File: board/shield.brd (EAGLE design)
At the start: 66 x 57.8 mm, 45 parts, among them IC1 LM75, J1 22-05-7048-04, J2 22-05-7028-02, J4 POWER_JACKPTH, K1 G5L, T1 BC817, U1 LM2596S-5.0

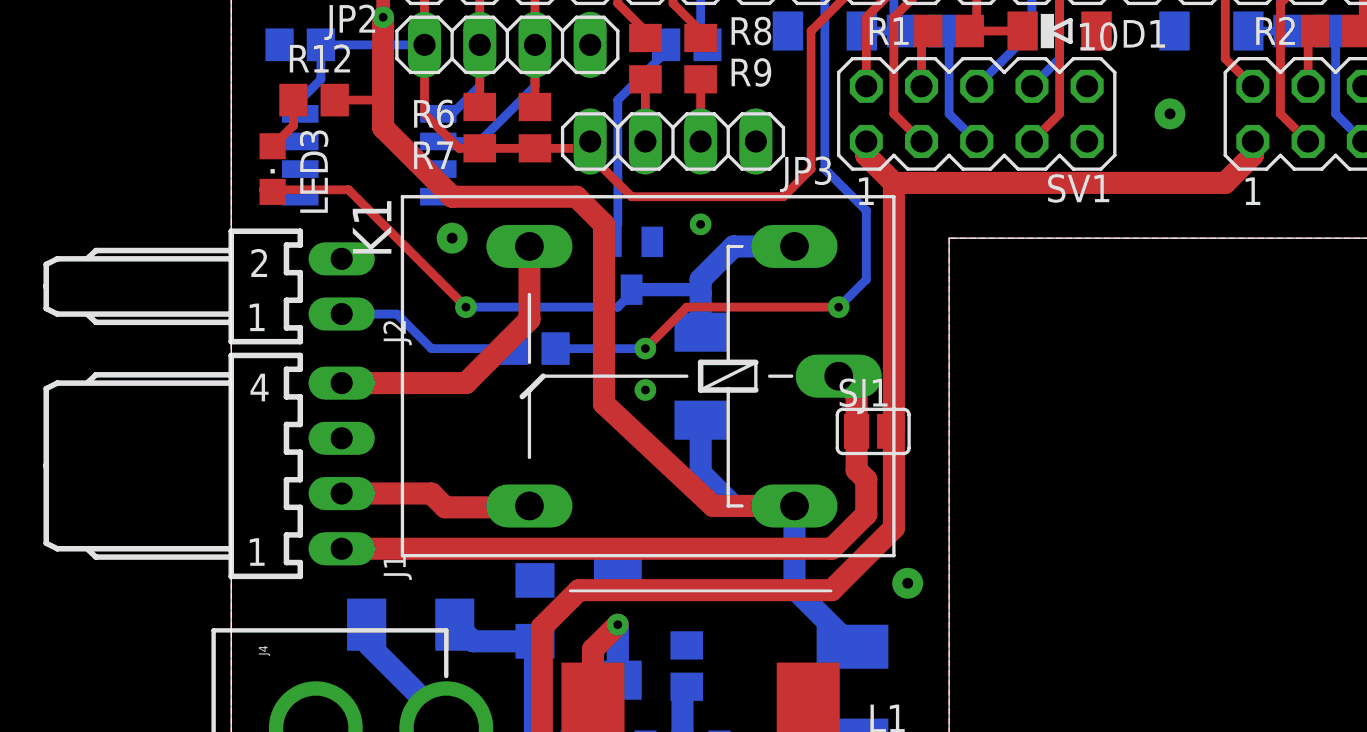
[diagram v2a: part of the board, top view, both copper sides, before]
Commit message: Fixed DRC Error, minor changes
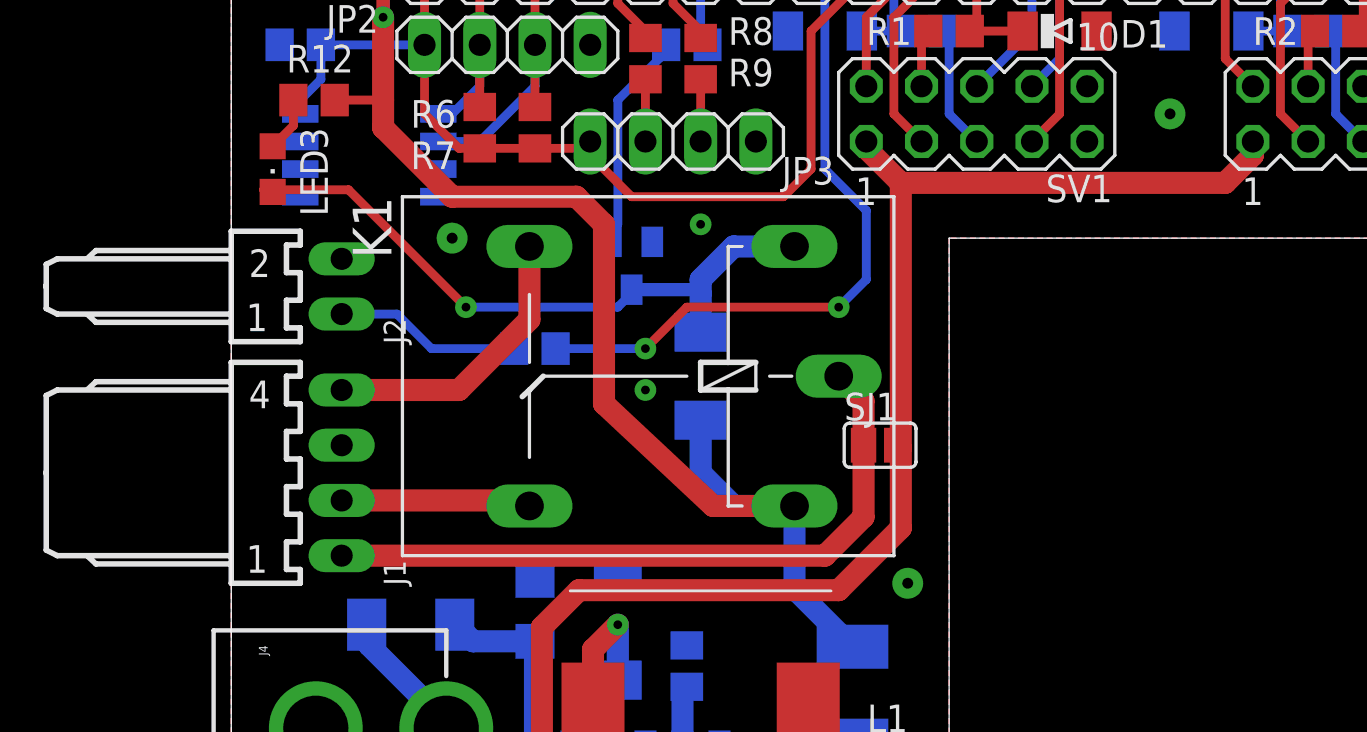
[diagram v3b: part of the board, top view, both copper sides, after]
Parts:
- moved SJ1 0.71 mm to (29.8, 30.5)
- moved J1 0.32 mm to (5.08, 29.2)
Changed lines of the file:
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@@
 <attribute name="PROD_ID" value="CONN-08197" x="-3.81" y="17.4625" size="1.778" layer="27" rot="R270" display="off"/>
 </element>
-<element name="J1" library="con-molex" package="7395-04" value="22-05-7048-04" x="5.08" y="29.5275" rot="R270">
-<attribute name="MF" value="" x="5.08" y="29.5275" size="1.778" layer="27" rot="R270" display="off"/>
-<attribute name="MPN" value="" x="5.08" y="29.5275" size="1.778" layer="27" rot="R270" display="off"/>
-<attribute name="OC_FARNELL" value="unknown" x="5.08" y="29.5275" size="1.778" layer="27" rot="R270" display="off"/>
-<attribute name="OC_NEWARK" value="unknown" x="5.08" y="29.5275" size="1.778" layer="27" rot="R270" display="off"/>
+<element name="J1" library="con-molex" package="7395-04" value="22-05-7048-04" x="5.08" y="29.21" rot="R270">
+<attribute name="MF" value="" x="5.08" y="29.21" size="1.778" layer="27" rot="R270" display="off"/>
+<attribute name="MPN" value="" x="5.08" y="29.21" size="1.778" layer="27" rot="R270" display="off"/>
+<attribute name="OC_FARNELL" value="unknown" x="5.08" y="29.21" size="1.778" layer="27" rot="R270" display="off"/>
+<attribute name="OC_NEWARK" value="unknown" x="5.08" y="29.21" size="1.778" layer="27" rot="R270" display="off"/>
 </element>
-<element name="SJ1" library="jumper" package="SJ" value="" x="29.5275" y="31.115"/>
+<element name="SJ1" library="jumper" package="SJ" value="" x="29.845" y="30.48"/>
 </elements>
 <signals>
@@
 <contactref element="SV1" pad="1"/>
 <contactref element="SV2" pad="1"/>
-<wire x1="29.21" y1="43.815" x2="30.48" y2="42.545" width="1.016" layer="1"/>
-<wire x1="29.21" y1="44.45" x2="29.21" y2="43.815" width="1.016" layer="1"/>
+<wire x1="29.21" y1="44.1325" x2="30.7975" y2="42.545" width="1.016" layer="1"/>
+<wire x1="29.21" y1="44.45" x2="29.21" y2="44.1325" width="1.016" layer="1"/>
 <wire x1="46.99" y1="44.45" x2="46.99" y2="43.815" width="1.016" layer="1"/>
 <wire x1="46.99" y1="43.815" x2="45.72" y2="42.545" width="1.016" layer="1"/>
-<wire x1="45.72" y1="42.545" x2="30.48" y2="42.545" width="1.016" layer="1"/>
-<wire x1="30.48" y1="42.545" x2="30.48" y2="31.4325" width="1.016" layer="1"/>
-<wire x1="30.48" y1="31.3055" x2="30.48" y2="26.67" width="1.016" layer="1"/>
-<wire x1="30.48" y1="26.67" x2="27.6225" y2="23.8125" width="1.016" layer="1"/>
-<wire x1="15.995" y1="23.8125" x2="27.6225" y2="23.8125" width="1.016" layer="1"/>
+<wire x1="45.72" y1="42.545" x2="30.7975" y2="42.545" width="1.016" layer="1"/>
+<wire x1="30.7975" y1="42.545" x2="30.7975" y2="30.353" width="1.016" layer="1"/>
+<wire x1="30.7975" y1="30.353" x2="30.7975" y2="26.67" width="1.016" layer="1"/>
+<wire x1="30.7975" y1="26.67" x2="27.94" y2="23.8125" width="1.016" layer="1"/>
+<wire x1="15.995" y1="23.8125" x2="27.94" y2="23.8125" width="1.016" layer="1"/>
 <wire x1="12.065" y1="9.4742" x2="12.065" y2="12.065" width="1.016" layer="1"/>
 <wire x1="11.125" y1="21.46" x2="10.36" y2="22.225" width="1.016" layer="16"/>
@@
 <wire x1="10.36" y1="22.225" x2="10.28" y2="22.225" width="0.4064" layer="16"/>
 <contactref element="SJ1" pad="2"/>
-<wire x1="30.2895" y1="31.115" x2="30.48" y2="31.3055" width="1.016" layer="1"/>
-<wire x1="30.48" y1="31.3055" x2="30.48" y2="31.4325" width="1.016" layer="1"/>
+<wire x1="30.607" y1="30.48" x2="30.7975" y2="30.353" width="1.016" layer="1"/>
 </signal>
 <signal name="N$4">
@@
 <signal name="NO">
 <contactref element="K1" pad="S"/>
-<wire x1="5.08" y1="33.3375" x2="10.795" y2="33.3375" width="1.016" layer="1"/>
-<wire x1="10.795" y1="33.3375" x2="13.716" y2="36.2585" width="1.016" layer="1"/>
+<wire x1="5.08" y1="33.02" x2="10.4775" y2="33.02" width="1.016" layer="1"/>
+<wire x1="10.4775" y1="33.02" x2="13.716" y2="36.2585" width="1.016" layer="1"/>
 <wire x1="13.716" y1="36.2585" x2="13.716" y2="39.624" width="1.016" layer="1"/>
 <contactref element="J1" pad="4"/>
@@
 <signal name="NC">
 <contactref element="K1" pad="O"/>
-<wire x1="5.08" y1="28.2575" x2="9.2075" y2="28.2575" width="1.016" layer="1"/>
-<wire x1="9.2075" y1="28.2575" x2="9.8425" y2="27.6225" width="1.016" layer="1"/>
-<wire x1="9.8425" y1="27.6225" x2="13.6525" y2="27.6225" width="1.016" layer="1"/>
-<wire x1="13.6525" y1="27.6225" x2="13.716" y2="27.686" width="1.016" layer="1"/>
+<wire x1="5.08" y1="27.94" x2="13.335" y2="27.94" width="1.016" layer="1"/>
+<wire x1="13.335" y1="27.94" x2="13.716" y2="27.686" width="1.016" layer="1"/>
 <contactref element="J1" pad="2"/>
 </signal>
@@
 <contactref element="J1" pad="1"/>
 <contactref element="SJ1" pad="1"/>
-<wire x1="5.08" y1="25.7175" x2="27.6225" y2="25.7175" width="1.016" layer="1"/>
-<wire x1="27.6225" y1="25.7175" x2="29.21" y2="27.305" width="1.016" layer="1"/>
-<wire x1="29.21" y1="27.305" x2="29.21" y2="28.8925" width="1.016" layer="1"/>
-<wire x1="29.21" y1="28.8925" x2="28.7655" y2="29.337" width="1.016" layer="1"/>
-<wire x1="28.7655" y1="29.337" x2="28.7655" y2="31.115" width="1.016" layer="1"/>
-<wire x1="27.94" y1="33.655" x2="28.7655" y2="32.8295" width="1.016" layer="1"/>
-<wire x1="28.7655" y1="32.8295" x2="28.7655" y2="31.115" width="1.016" layer="1"/>
+<wire x1="5.08" y1="25.4" x2="27.305" y2="25.4" width="1.016" layer="1"/>
+<wire x1="29.083" y1="30.2895" x2="29.083" y2="30.48" width="1.016" layer="1"/>
+<wire x1="27.305" y1="25.4" x2="29.083" y2="27.178" width="1.016" layer="1"/>
+<wire x1="29.083" y1="27.178" x2="29.083" y2="30.48" width="1.016" layer="1"/>
+<wire x1="29.083" y1="30.48" x2="29.083" y2="32.512" width="1.016" layer="1"/>
+<wire x1="29.083" y1="32.512" x2="27.94" y2="33.655" width="1.016" layer="1"/>
 </signal>
 </signals>

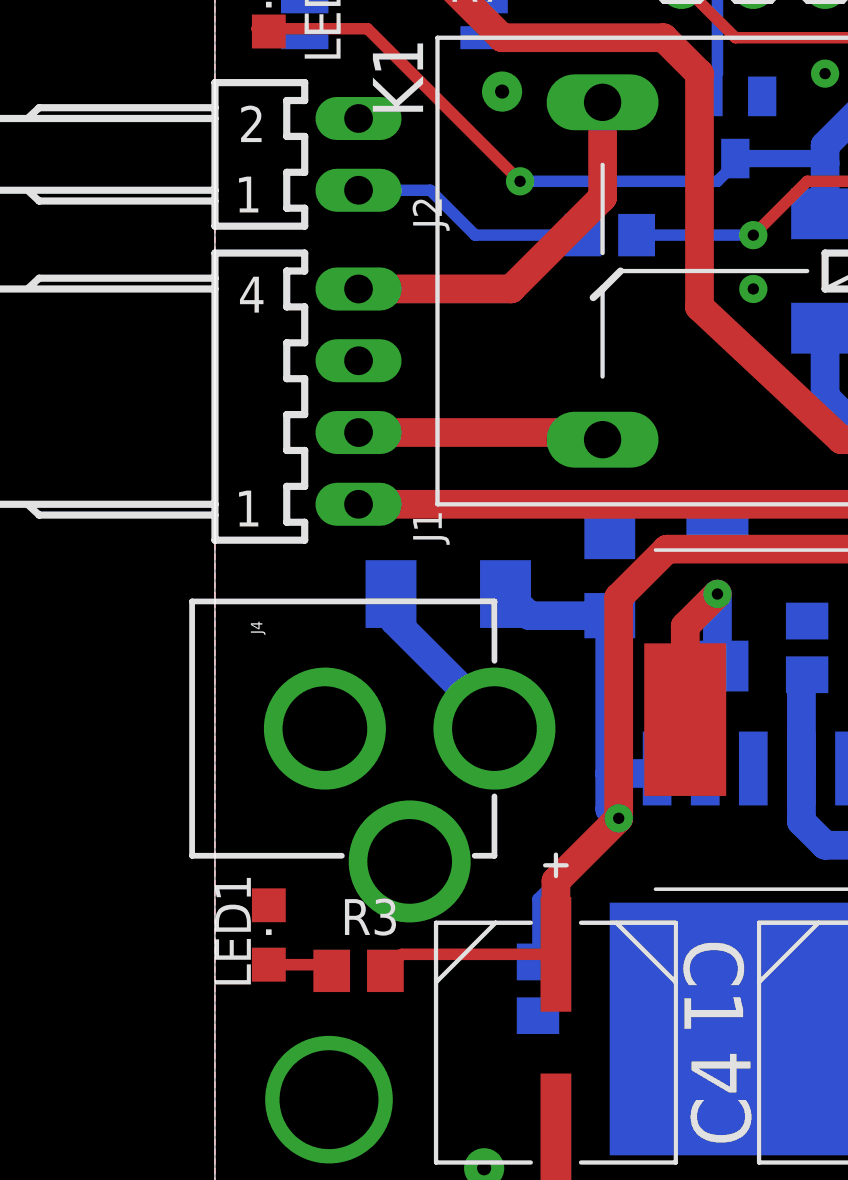
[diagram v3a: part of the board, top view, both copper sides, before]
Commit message: Labels position optimized
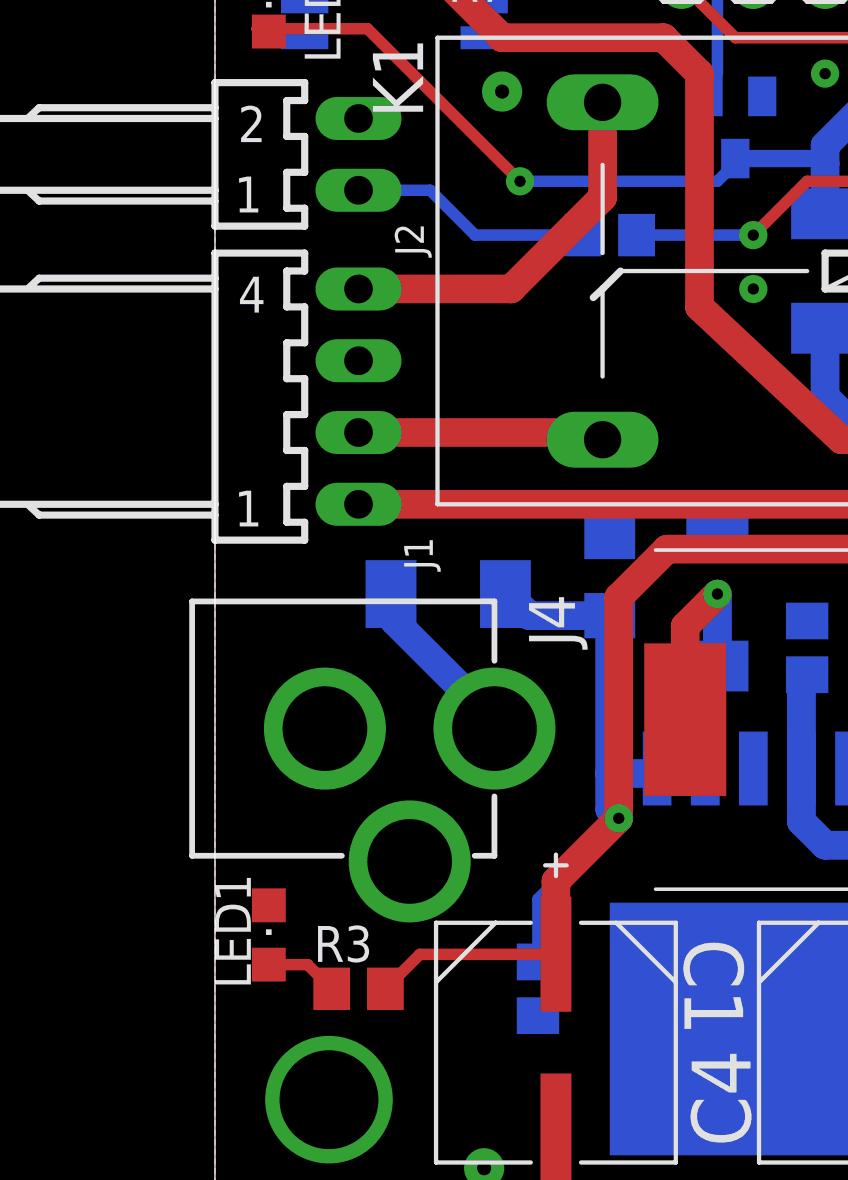
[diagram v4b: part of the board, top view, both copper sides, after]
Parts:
- moved R3 0.63 mm to (5.08, 8.26)
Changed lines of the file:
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@@
 <layers>
 <layer number="1" name="Top" color="4" fill="1" visible="yes" active="yes"/>
-<layer number="16" name="Bottom" color="1" fill="1" visible="yes" active="yes"/>
+<layer number="16" name="Bottom" color="1" fill="1" visible="no" active="yes"/>
 <layer number="17" name="Pads" color="2" fill="1" visible="yes" active="yes"/>
 <layer number="18" name="Vias" color="2" fill="1" visible="yes" active="yes"/>
@@
 <layer number="20" name="Dimension" color="15" fill="1" visible="yes" active="yes"/>
 <layer number="21" name="tPlace" color="7" fill="1" visible="yes" active="yes"/>
-<layer number="22" name="bPlace" color="7" fill="1" visible="yes" active="yes"/>
+<layer number="22" name="bPlace" color="7" fill="1" visible="no" active="yes"/>
 <layer number="23" name="tOrigins" color="15" fill="1" visible="yes" active="yes"/>
-<layer number="24" name="bOrigins" color="15" fill="1" visible="yes" active="yes"/>
-<layer number="25" name="tNames" color="7" fill="1" visible="no" active="yes"/>
+<layer number="24" name="bOrigins" color="15" fill="1" visible="no" active="yes"/>
+<layer number="25" name="tNames" color="7" fill="1" visible="yes" active="yes"/>
 <layer number="26" name="bNames" color="7" fill="1" visible="no" active="yes"/>
 <layer number="27" name="tValues" color="7" fill="1" visible="no" active="yes"/>
@@
 <layer number="50" name="dxf" color="7" fill="1" visible="no" active="no"/>
 <layer number="51" name="tDocu" color="7" fill="1" visible="yes" active="yes"/>
-<layer number="52" name="bDocu" color="7" fill="1" visible="yes" active="yes"/>
+<layer number="52" name="bDocu" color="7" fill="1" visible="no" active="yes"/>
 <layer number="53" name="tPadExt" color="7" fill="1" visible="no" active="no"/>
 <layer number="54" name="bPadExt" color="1" fill="1" visible="no" active="no"/>
@@
 <layer number="99" name="SpiceOrder" color="5" fill="1" visible="no" active="no"/>
 <layer number="100" name="Muster" color="7" fill="1" visible="no" active="no"/>
-<layer number="101" name="Patch_Top" color="12" fill="4" visible="yes" active="yes"/>
-<layer number="102" name="Vscore" color="7" fill="1" visible="yes" active="yes"/>
-<layer number="103" name="tMap" color="7" fill="1" visible="yes" active="yes"/>
-<layer number="104" name="Name" color="16" fill="1" visible="yes" active="yes"/>
+<layer number="101" name="Patch_Top" color="12" fill="4" visible="no" active="yes"/>
+<layer number="102" name="Vscore" color="7" fill="1" visible="no" active="yes"/>
+<layer number="103" name="tMap" color="7" fill="1" visible="no" active="yes"/>
+<layer number="104" name="Name" color="16" fill="1" visible="no" active="yes"/>
 <layer number="105" name="tPlate" color="7" fill="1" visible="yes" active="yes"/>
-<layer number="106" name="bPlate" color="7" fill="1" visible="yes" active="yes"/>
+<layer number="106" name="bPlate" color="7" fill="1" visible="no" active="yes"/>
 <layer number="107" name="Crop" color="7" fill="1" visible="yes" active="yes"/>
 <layer number="108" name="tplace-old" color="10" fill="1" visible="yes" active="yes"/>
@@
 <attribute name="VALUE" x="16.51" y="41.91" size="1.27" layer="28" rot="MR180"/>
 </element>
-<element name="R3" library="rcl" package="R0805" value="5K6" x="5.08" y="8.89" smashed="yes">
-<attribute name="NAME" x="4.445" y="10.16" size="1.27" layer="25"/>
-<attribute name="VALUE" x="4.445" y="6.35" size="1.27" layer="27"/>
+<element name="R3" library="rcl" package="R0805" value="5K6" x="5.08" y="8.255" smashed="yes">
+<attribute name="NAME" x="3.4925" y="9.2075" size="1.27" layer="25"/>
+<attribute name="VALUE" x="4.445" y="5.715" size="1.27" layer="27"/>
 </element>
 <element name="R10" library="rcl" package="R0805" value="560R" x="29.21" y="7.62" smashed="yes" rot="R270">
@@
 </element>
 <element name="PCB1" library="e14_Rpi3_RevA" package="RPI3" value="RPI3" x="122.36" y="-1.375" rot="R90"/>
-<element name="J2" library="con-molex" package="7395-02" value="22-05-7028-02" x="5.08" y="37.7825" rot="R270">
+<element name="J2" library="con-molex" package="7395-02" value="22-05-7028-02" x="5.08" y="37.7825" smashed="yes" rot="R270">
 <attribute name="OC_FARNELL" value="9731601" x="5.08" y="37.7825" size="1.778" layer="27" rot="R270" display="off"/>
 <attribute name="MPN" value="" x="5.08" y="37.7825" size="1.778" layer="27" rot="R270" display="off"/>
 <attribute name="OC_NEWARK" value="unknown" x="5.08" y="37.7825" size="1.778" layer="27" rot="R270" display="off"/>
 <attribute name="MF" value="" x="5.08" y="37.7825" size="1.778" layer="27" rot="R270" display="off"/>
+<attribute name="NAME" x="7.3929" y="34.1899" size="1.016" layer="25" ratio="10" rot="R90"/>
+<attribute name="VALUE" x="2.6401" y="34.3804" size="0.8128" layer="27" ratio="10" rot="R180"/>
 </element>
 <element name="SV1" library="con-lstb" package="MA05-2" value="S2G10" x="34.29" y="45.72" smashed="yes">
@@
 </element>
 <element name="C6" library="rcl" package="C0805" value="100n" x="3.175" y="48.895" rot="MR180"/>
-<element name="J4" library="SparkFun-Connectors" package="POWER_JACK_PTH" value="POWER_JACKPTH" x="-3.81" y="17.4625" rot="R270">
+<element name="J4" library="SparkFun-Connectors" package="POWER_JACK_PTH" value="POWER_JACKPTH" x="-3.81" y="17.4625" smashed="yes" rot="R270">
 <attribute name="PROD_ID" value="CONN-08197" x="-3.81" y="17.4625" size="1.778" layer="27" rot="R270" display="off"/>
-</element>
-<element name="J1" library="con-molex" package="7395-04" value="22-05-7048-04" x="5.08" y="29.21" rot="R270">
+<attribute name="NAME" x="11.1125" y="22.225" size="1.6256" layer="25" rot="R270"/>
+<attribute name="VALUE" x="0" y="21.2725" size="0.4064" layer="27" rot="R270"/>
+</element>
+<element name="J1" library="con-molex" package="7395-04" value="22-05-7048-04" x="5.08" y="29.21" smashed="yes" rot="R270">
 <attribute name="MF" value="" x="5.08" y="29.21" size="1.778" layer="27" rot="R270" display="off"/>
 <attribute name="MPN" value="" x="5.08" y="29.21" size="1.778" layer="27" rot="R270" display="off"/>
 <attribute name="OC_FARNELL" value="unknown" x="5.08" y="29.21" size="1.778" layer="27" rot="R270" display="off"/>
 <attribute name="OC_NEWARK" value="unknown" x="5.08" y="29.21" size="1.778" layer="27" rot="R270" display="off"/>
+<attribute name="NAME" x="7.7104" y="23.0774" size="1.016" layer="25" ratio="10" rot="R90"/>
+<attribute name="VALUE" x="2.6401" y="23.2679" size="0.8128" layer="27" ratio="10" rot="R180"/>
 </element>
 <element name="SJ1" library="jumper" package="SJ" value="" x="29.845" y="30.48"/>
@@
 <wire x1="13.97" y1="15.875" x2="13.97" y2="21.46" width="1.016" layer="16"/>
 <wire x1="13.97" y1="21.46" x2="11.125" y2="21.46" width="1.016" layer="16"/>
-<wire x1="12.065" y1="9.4742" x2="6.6142" y2="9.4742" width="0.4064" layer="1"/>
-<wire x1="6.6142" y1="9.4742" x2="6.03" y2="8.89" width="0.4064" layer="1"/>
+<wire x1="12.065" y1="9.4742" x2="7.2492" y2="9.4742" width="0.4064" layer="1"/>
+<wire x1="7.2492" y1="9.4742" x2="6.03" y2="8.255" width="0.4064" layer="1"/>
 <wire x1="12.065" y1="8.89" x2="12.065" y2="9.4742" width="1.016" layer="1"/>
 <contactref element="SV1" pad="1"/>
@@
 <contactref element="R3" pad="1"/>
 <contactref element="LED1" pad="A"/>
-<wire x1="1.905" y1="9.11" x2="3.91" y2="9.11" width="0.4064" layer="1"/>
-<wire x1="3.91" y1="9.11" x2="4.13" y2="8.89" width="0.4064" layer="1"/>
+<wire x1="1.905" y1="9.11" x2="3.275" y2="9.11" width="0.4064" layer="1"/>
+<wire x1="3.275" y1="9.11" x2="4.13" y2="8.255" width="0.4064" layer="1"/>
 </signal>
 <signal name="N$3">
